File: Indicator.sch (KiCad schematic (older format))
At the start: 23 parts, among them Q1 BC817-25LT1G, Q2 BC817-25LT1G, U1 CC56-12SURKWA, U2 CC56-12SURKWA, U3 MAX7219EWG+T, U4 BC56-12SURKWA, U5 SC56-11SRWA, U6 MAX7219EWG+T, U7 CC56-12SURKWA

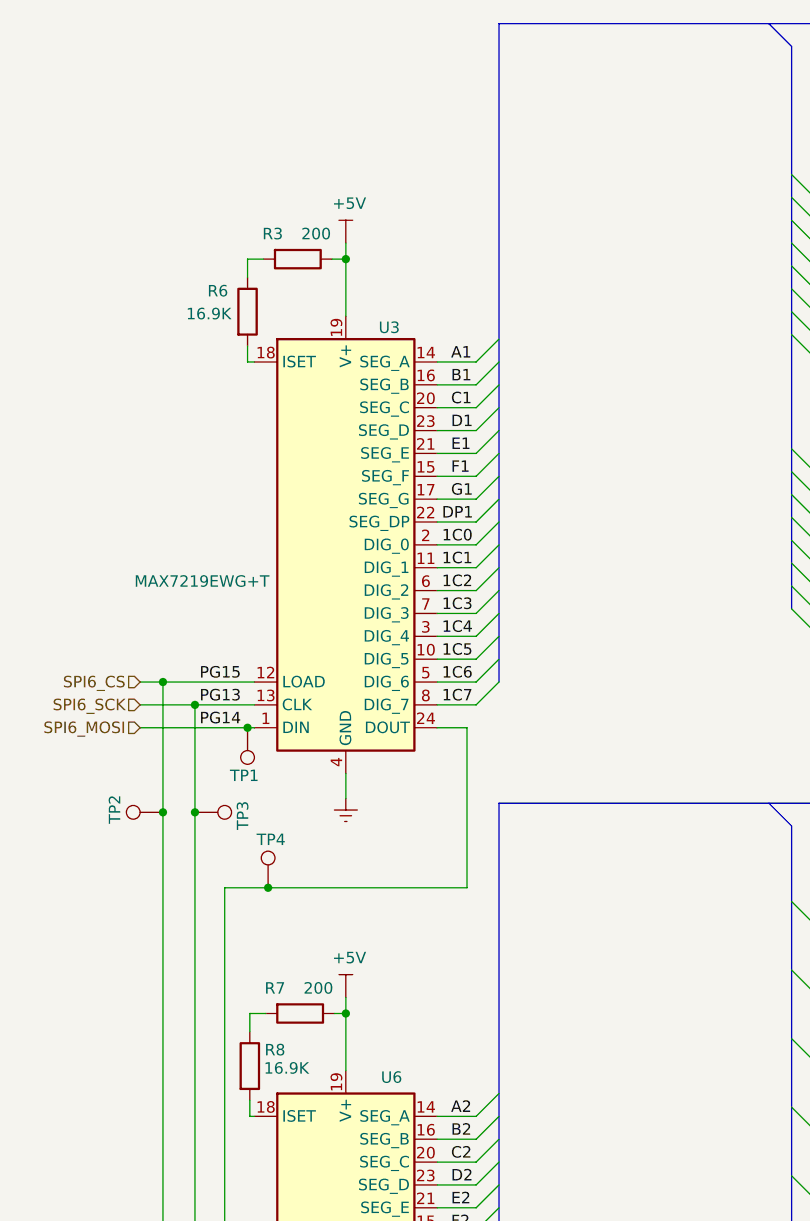
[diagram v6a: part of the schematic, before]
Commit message: Indicators layout finished
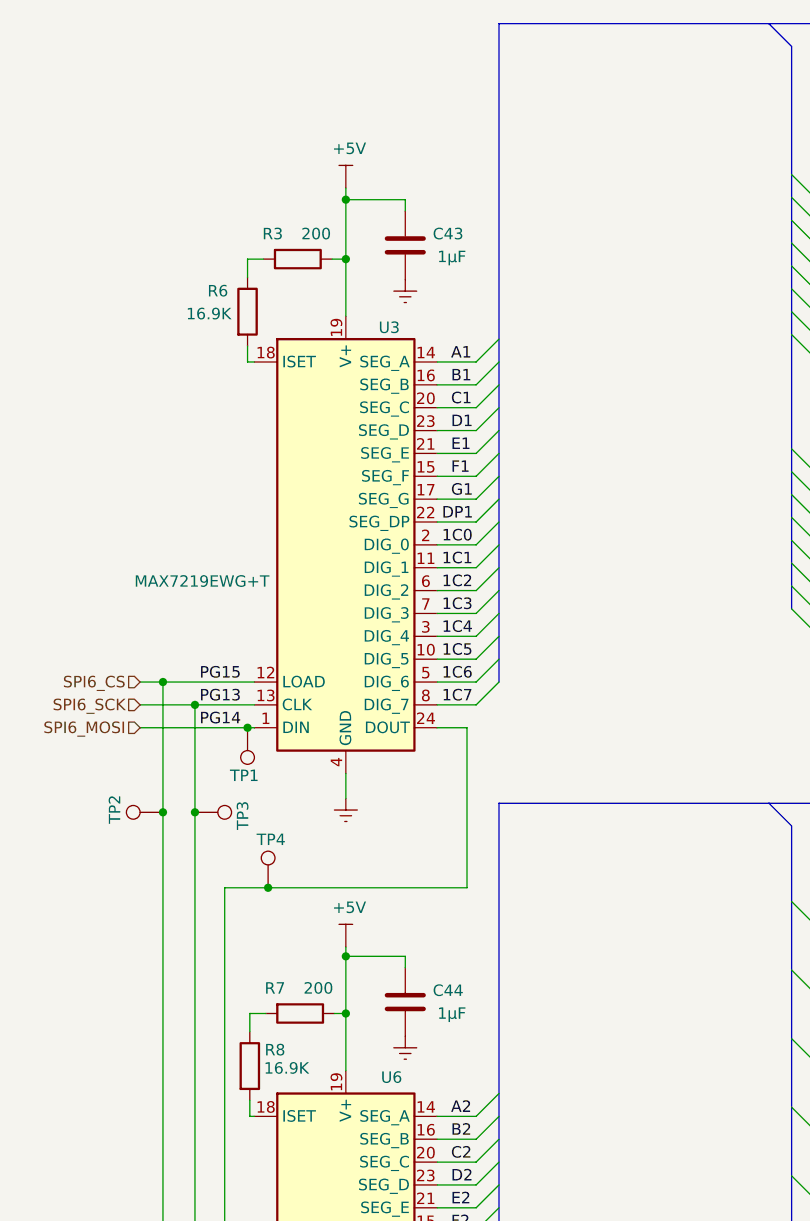
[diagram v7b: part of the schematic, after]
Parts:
- added C43, C44: 1µF, Capacitor_SMD:C_0603_1608Metric_Pad1.08x0.95mm_HandSolder, symbol Device:C
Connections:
- net +5V: now also C43.1, C44.1
- net GNDREF: now also C43.2, C44.2
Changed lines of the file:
@@
 L SVIELCOM_Library:+5V #PWR07
 U 1 1 60C625DC
-P 1880 4950
-F 0 "#PWR07" H 1880 4800 50  0001 C CNN
-F 1 "+5V" H 1895 5123 50  0000 C CNN
-F 2 "" H 1880 4950 50  0001 C CNN
-F 3 "" H 1880 4950 50  0001 C CNN
-	1    1880 4950
+P 1880 4730
+F 0 "#PWR07" H 1880 4580 50  0001 C CNN
+F 1 "+5V" H 1895 4903 50  0000 C CNN
+F 2 "" H 1880 4730 50  0001 C CNN
+F 3 "" H 1880 4730 50  0001 C CNN
+	1    1880 4730
 	1    0    0    -1
 $EndComp
@@
 L SVIELCOM_Library:+5V #PWR03
 U 1 1 60C9A9E7
-P 1880 1650
-F 0 "#PWR03" H 1880 1500 50  0001 C CNN
-F 1 "+5V" H 1895 1823 50  0000 C CNN
-F 2 "" H 1880 1650 50  0001 C CNN
-F 3 "" H 1880 1650 50  0001 C CNN
-	1    1880 1650
+P 1880 1410
+F 0 "#PWR03" H 1880 1260 50  0001 C CNN
+F 1 "+5V" H 1895 1583 50  0000 C CNN
+F 2 "" H 1880 1410 50  0001 C CNN
+F 3 "" H 1880 1410 50  0001 C CNN
+	1    1880 1410
 	1    0    0    -1
 $EndComp
@@
 "EAST"
 Wire Wire Line
-	1880 1650 1880 1720
+	1880 1410 1880 1460
 $Comp
 L Device:R R?
@@
 	1880 1720 1880 1970
 Wire Wire Line
-	1880 4950 1880 5020
+	1880 4730 1880 4770
 $Comp
 L Device:R R?
@@
 Wire Wire Line
 	1450 3770 1480 3770
+$Comp
+L Device:C C?
+U 1 1 60F62724
+P 2140 1660
+AR Path="/60F62724" Ref="C?"  Part="1"
+AR Path="/60A03F8A/60F62724" Ref="C?"  Part="1"
+AR Path="/60D8C564/60F62724" Ref="C?"  Part="1"
+AR Path="/608C8099/60F62724" Ref="C43"  Part="1"
+F 0 "C43" H 2260 1710 50  0000 L CNN
+F 1 "1µF" H 2280 1610 50  0000 L CNN
+F 2 "Capacitor_SMD:C_0603_1608Metric_Pad1.08x0.95mm_HandSolder" H 2178 1510 50  0001 C CNN
+F 3 "http://www.farnell.com/datasheets/2710676.pdf" H 2140 1660 50  0001 C CNN
+F 4 "CL10B105KA8NNNC" H 2140 1660 50  0001 C CNN "Type"
+	1    2140 1660
+	1    0    0    -1
+$EndComp
+$Comp
+L power:GNDREF #PWR?
+U 1 1 60F6272A
+P 2140 1810
+AR Path="/60F6272A" Ref="#PWR?"  Part="1"
+AR Path="/60A03F8A/60F6272A" Ref="#PWR?"  Part="1"
+AR Path="/60D8C564/60F6272A" Ref="#PWR?"  Part="1"
+AR Path="/608C8099/60F6272A" Ref="#PWR047"  Part="1"
+F 0 "#PWR047" H 2140 1560 50  0001 C CNN
+F 1 "GNDREF" V 2145 1682 50  0001 R CNN
+F 2 "" H 2140 1810 50  0001 C CNN
+F 3 "" H 2140 1810 50  0001 C CNN
+	1    2140 1810
+	1    0    0    -1
+$EndComp
+Wire Wire Line
+	1880 1460 2140 1460
+Wire Wire Line
+	2140 1460 2140 1510
+Connection ~ 1880 1460
+Wire Wire Line
+	1880 1460 1880 1720
+$Comp
+L Device:C C?
+U 1 1 60F85DF0
+P 2140 4970
+AR Path="/60F85DF0" Ref="C?"  Part="1"
+AR Path="/60A03F8A/60F85DF0" Ref="C?"  Part="1"
+AR Path="/60D8C564/60F85DF0" Ref="C?"  Part="1"
+AR Path="/608C8099/60F85DF0" Ref="C44"  Part="1"
+F 0 "C44" H 2260 5020 50  0000 L CNN
+F 1 "1µF" H 2280 4920 50  0000 L CNN
+F 2 "Capacitor_SMD:C_0603_1608Metric_Pad1.08x0.95mm_HandSolder" H 2178 4820 50  0001 C CNN
+F 3 "http://www.farnell.com/datasheets/2710676.pdf" H 2140 4970 50  0001 C CNN
+F 4 "CL10B105KA8NNNC" H 2140 4970 50  0001 C CNN "Type"
+	1    2140 4970
+	1    0    0    -1
+$EndComp
+$Comp
+L power:GNDREF #PWR?
+U 1 1 60F85DF6
+P 2140 5120
+AR Path="/60F85DF6" Ref="#PWR?"  Part="1"
+AR Path="/60A03F8A/60F85DF6" Ref="#PWR?"  Part="1"
+AR Path="/60D8C564/60F85DF6" Ref="#PWR?"  Part="1"
+AR Path="/608C8099/60F85DF6" Ref="#PWR048"  Part="1"
+F 0 "#PWR048" H 2140 4870 50  0001 C CNN
+F 1 "GNDREF" V 2145 4992 50  0001 R CNN
+F 2 "" H 2140 5120 50  0001 C CNN
+F 3 "" H 2140 5120 50  0001 C CNN
+	1    2140 5120
+	1    0    0    -1
+$EndComp
+Wire Wire Line
+	1880 4770 2140 4770
+Wire Wire Line
+	2140 4770 2140 4820
+Connection ~ 1880 4770
+Wire Wire Line
+	1880 4770 1880 5020
 Wire Bus Line
 	2550 690  6810 690

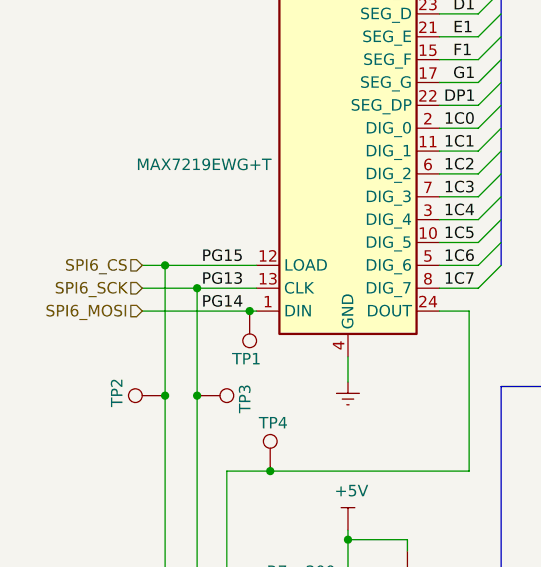
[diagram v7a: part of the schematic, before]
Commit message: SPI6 changed to SPI1
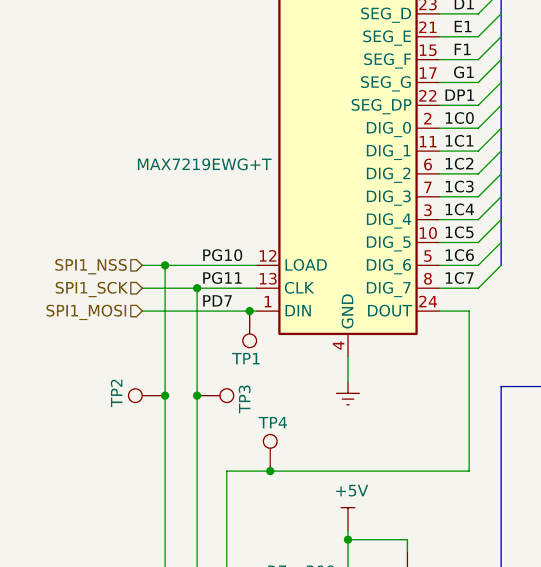
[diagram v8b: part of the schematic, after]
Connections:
- net SPI6_CS renamed SPI1_NSS
- net SPI6_MOSI renamed SPI1_MOSI
- net SPI6_SCK renamed SPI1_SCK
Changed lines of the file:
@@
 	1880 7270 1880 7380
 Text HLabel 980  3570 0    50   Input ~ 0
-SPI6_CS
+SPI1_NSS
 Wire Wire Line
 	980  3570 1080 3570
 Connection ~ 1080 3570
 Text Label 1240 3570 0    50   ~ 0
-PG15
+PG10
 Text HLabel 980  3670 0    50   Input ~ 0
-SPI6_SCK
+SPI1_SCK
 Wire Wire Line
 	980  3670 1220 3670
 Connection ~ 1220 3670
 Text HLabel 980  3770 0    50   Input ~ 0
-SPI6_MOSI
+SPI1_MOSI
 Wire Wire Line
 	980  3770 1450 3770
 Text Label 1240 3670 0    50   ~ 0
-PG13
+PG11
 Text Label 1240 3770 0    50   ~ 0
-PG14
+PD7
 $Comp
 L Device:LED D1
